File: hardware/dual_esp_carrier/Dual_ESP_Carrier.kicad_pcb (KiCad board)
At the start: 2 copper layers, 100 x 100 mm, 25 parts, among them J1 ESP32_lafvin, J2 ESP32_B_LANDSCAPE, J3 SX1278_LORA_2x4, J6 GPS_LC29H_7PIN, SW1 subir ancora, SW2 MODE, SW3 largar ancora, SW4 BOOT

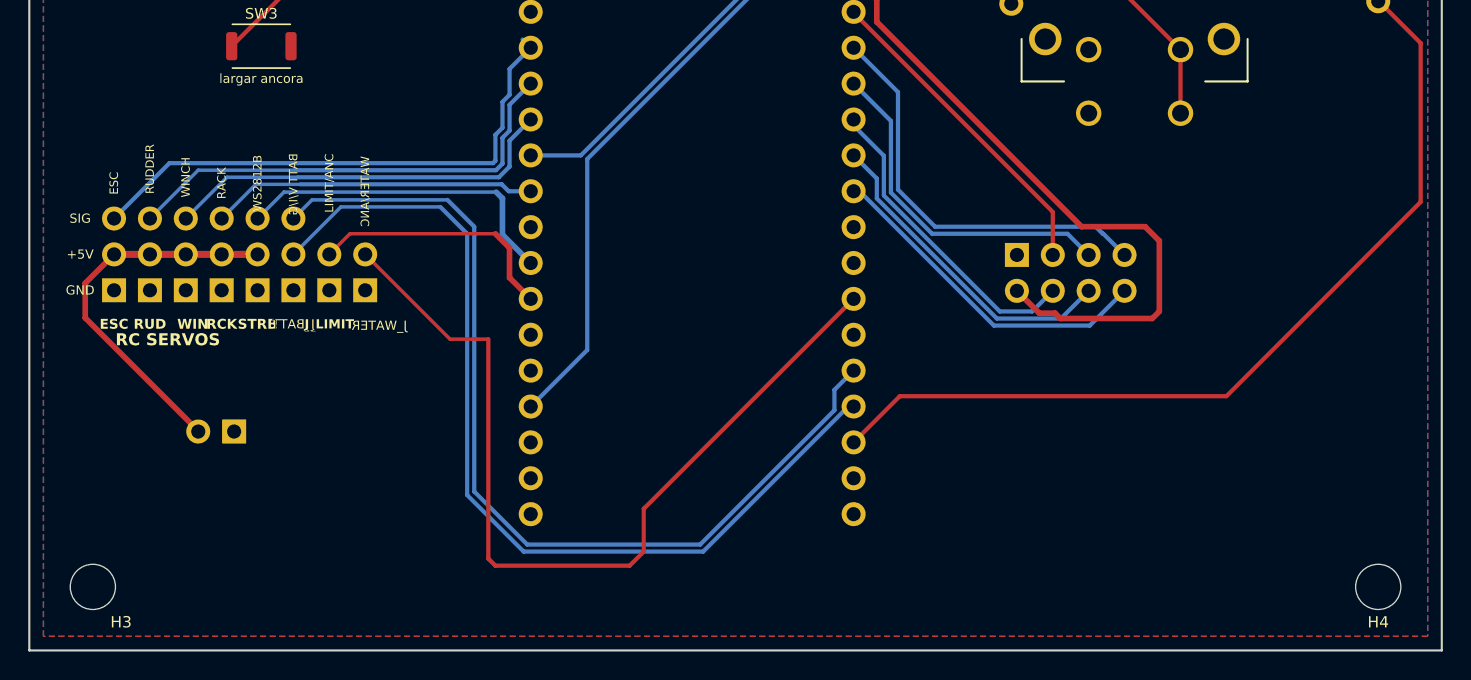
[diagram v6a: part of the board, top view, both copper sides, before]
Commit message: feat: add Hall sensor footprint and mounting holes to dual ESP carrier PCB
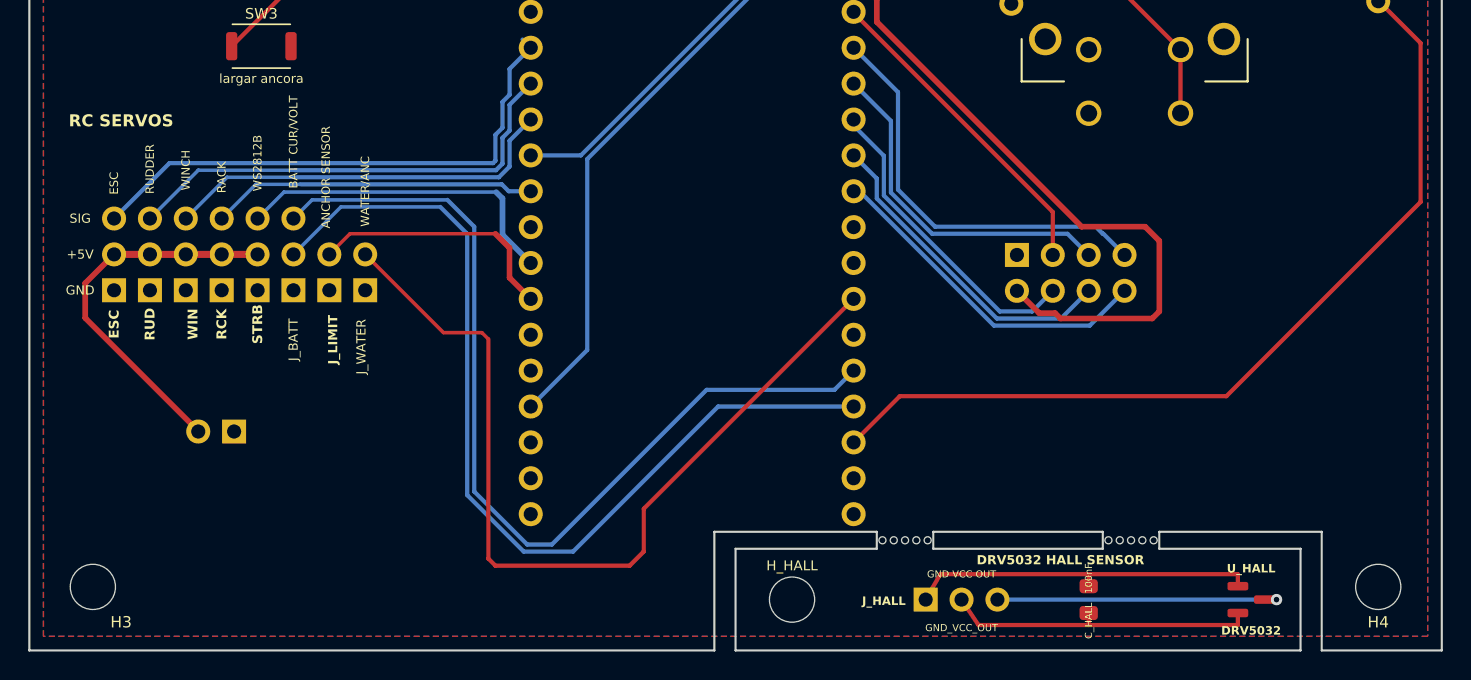
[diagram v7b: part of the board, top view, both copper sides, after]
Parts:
- added C_HALL: 100nF, Capacitor_SMD:C_0805_2012Metric, F.Cu at (75.0, 96.4)
- added H_HALL: M3_MOUNT, MountingHole:MountingHole_3.2mm_M3, F.Cu at (54.0, 96.4)
- added J_HALL: GND_VCC_OUT, Connector_PinHeader_2.54mm:PinHeader_1x03_P2.54mm_Horizontal, F.Cu at (66.0, 96.4)
- added STAMP: , MountingHole:MountingHole_0.5mm, F.Cu at (76.4, 92.2)
- added STAMP: , MountingHole:MountingHole_0.5mm, F.Cu at (62.0, 92.2)
- added STAMP: , MountingHole:MountingHole_0.5mm, F.Cu at (62.8, 92.2)
- added STAMP: , MountingHole:MountingHole_0.5mm, F.Cu at (79.6, 92.2)
- added STAMP: , MountingHole:MountingHole_0.5mm, F.Cu at (77.2, 92.2)
- added STAMP: , MountingHole:MountingHole_0.5mm, F.Cu at (63.6, 92.2)
- added STAMP: , MountingHole:MountingHole_0.5mm, F.Cu at (78.8, 92.2)
- added STAMP: , MountingHole:MountingHole_0.5mm, F.Cu at (61.2, 92.2)
- added STAMP: , MountingHole:MountingHole_0.5mm, F.Cu at (60.4, 92.2)
- added STAMP: , MountingHole:MountingHole_0.5mm, F.Cu at (78.0, 92.2)
- added U_HALL: DRV5032, Package_TO_SOT_SMD:SOT-23, F.Cu at (86.5, 96.4)
- J_BATT: value BATT V/I/G -> BATT CUR/VOLT
- J_LIMIT: value LIMIT/ANC -> ANCHOR SENSOR
- J_PWR_SRV: value 5V_SERVO -> 5V | 6V SBEC
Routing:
- net /HALL_GND: track 0.00 -> 24.8 mm
- net /HALL_VCC: track 0.00 -> 22.2 mm
- net /HALL_OUT: track 0.00 -> 20.6 mm, vias 0 -> 1
- net /BATT_VOLT: track 67.2 -> 66.4 mm
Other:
- outline, holes or cut-outs redrawn
- board text added: "DRV5032 HALL SENSOR"
- board text added: "GND VCC OUT"
- board text added: "WINCH SPOOL"

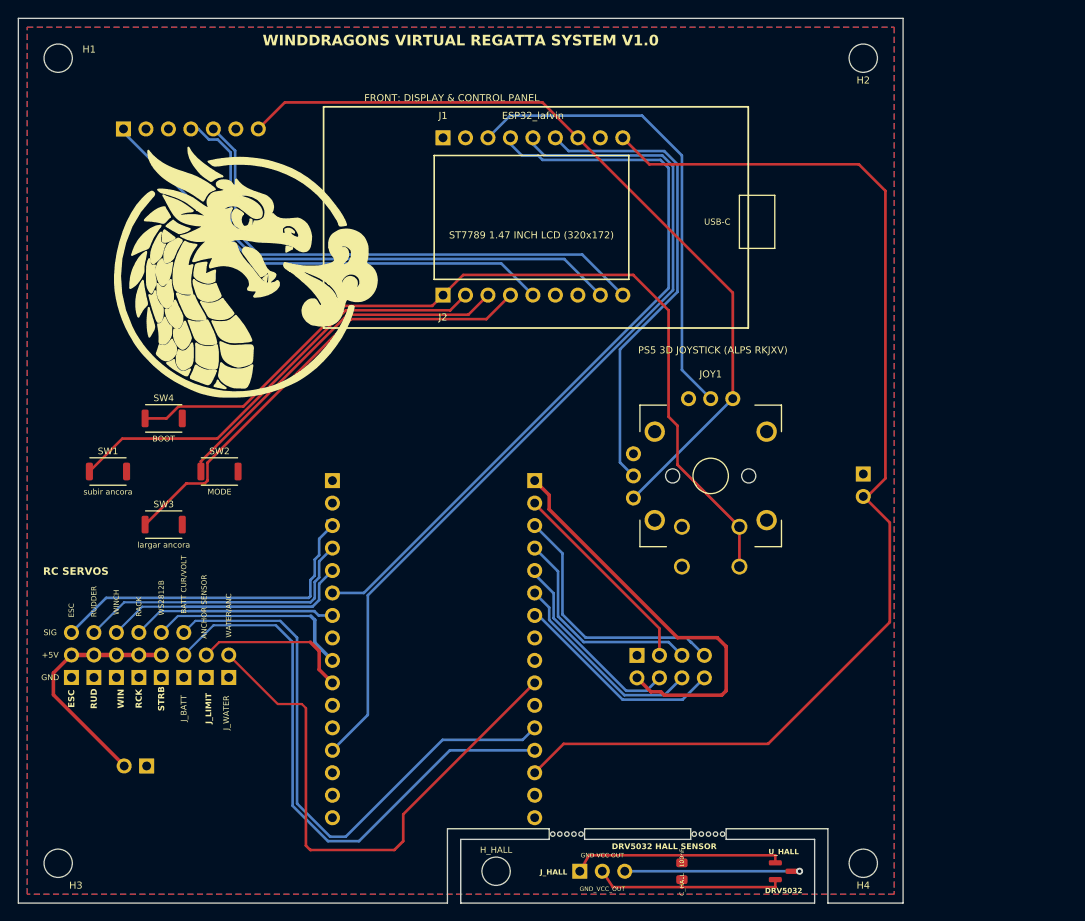
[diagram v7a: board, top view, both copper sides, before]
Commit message: update Dual_ESP_Carrier hardware files and pinout documentation for the anchor Hall sensor connector
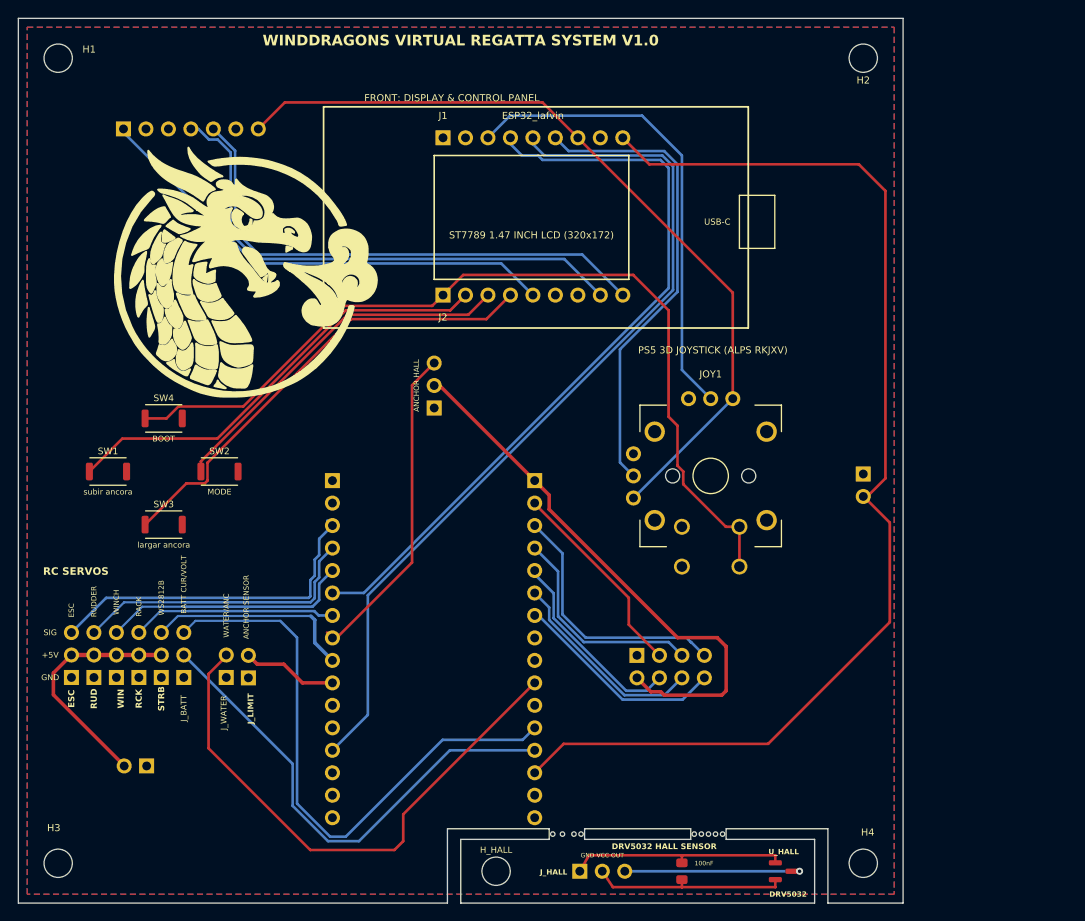
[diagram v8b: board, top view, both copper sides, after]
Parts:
- removed the STAMP at (62.0, 92.2)
- added HALL: ANCHOR HALL, Connector_PinHeader_2.54mm:PinHeader_1x03_P2.54mm_Vertical, F.Cu at (47.0, 44.0)
- moved J_LIMIT 4.76 mm to (26.0, 74.5)
- moved STAMP 0.30 mm to (61.5, 92.2)
- moved J_WATER 0.28 mm to (23.5, 74.5)
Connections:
- J_DK_R pad 8: (no net) -> /ANCHOR_HALL
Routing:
- net /ANCHOR_HALL: track 0.00 -> 37.0 mm
- net /+3V3_C6: track 46.4 -> 62.3 mm
- net /BATT_CURR: track 66.2 -> 55.4 mm
- net /ANCHOR_LIMIT: track 18.0 -> 10.8 mm
- net /IO9_BOOT: track 99.8 -> 100.7 mm
